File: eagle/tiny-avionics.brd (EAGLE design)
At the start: 65.8 x 25.4 mm, 67 parts, among them J1 USB-MICROB, J3 JST-PH-2-SMT-RA, U1 LP5907, U2 M25P10-AVMN6TP_TR, U3 LSM9DS0, U5 LTC1998, U6 ATMEGA32U4-AU, X1 8MHz

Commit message: Schematic work and created new device for 8-pin SPI memory chip.
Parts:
- removed C3: 4.7µ, rcl:C0603
- removed C4: .22µ, rcl:C0603
- removed R9: 0, rcl:R0603
- removed TP16, TP17: TPTP08R, testpad:TP08R
- removed U3: LSM9DS0, LSM9DS0:LGA-24
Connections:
- removed net GYR_EN: R9.1, U3.19
- removed net N$10: C4.2, U3.8
- removed net N$11: C4.1, U3.9
- removed net N$16: U3.14, U6.20
- removed net N$17: U3.13, U6.19
- removed net N$19: U3.11, U6.18
- removed net N$20: R9.2, U6.38
- removed net N$66: TP17.TP, U3.10
- removed net N$67: TP16.TP, U3.12
- removed net N$9: C3.2, U3.7
- net CLK: now also U$2.13; no longer U3.21
- net GND: now also U$2.2, U$2.3, U$2.6, U$2.7; no longer C3.1, U3.2, U3.3, U3.4, U3.5, U3.6
- net MISO: now also U$2.1; no longer U3.22, U3.23
- net MOSI: now also U$2.14; no longer U3.24
- net VCC: now also U$2.5, U$2.8; no longer U3.15, U3.16, U3.17, U3.18
- net XM_EN: now also U$2.12; no longer U3.20
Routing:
- net GYR_EN: track 28.1 -> 0.00 mm, vias 2 -> 0
- net N$17: track 18.6 -> 0.00 mm, vias 2 -> 0
- net N$16: track 18.4 -> 0.00 mm, vias 2 -> 0
- net N$19: track 14.6 -> 0.00 mm, vias 2 -> 0
- net VCC: track 141.1 -> 135.5 mm
- net GND: track 4.30 -> 0.00 mm
- net MISO: track 64.2 -> 60.5 mm
- net CLK: track 75.1 -> 71.8 mm
- net N$20: track 2.90 -> 0.00 mm
- net N$10: track 2.88 -> 0.00 mm
- net N$9: track 2.46 -> 0.00 mm
- net MOSI: track 73.6 -> 71.3 mm
- net N$11: track 1.77 -> 0.00 mm
- net N$67: track 1.42 -> 0.00 mm
- net N$66: track 1.34 -> 0.00 mm

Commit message: Working changes to schematic and layout.
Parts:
- removed U2: M25P10-AVMN6TP_TR, SOIC127P600X175-8N:SOIC127P600X175-8N
- added U$3: M25PX16, tinyav-lib:SO8
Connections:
- new net N$10: U$2.4, U6.18
- new net N$11: U$2.9, U6.19
- net CLK: now also U$3.6; no longer U2.6
- net GND: now also U$3.4; no longer U2.4
- net MEM_EN: now also U$3.1; no longer U2.1
- net MISO: now also U$3.2; no longer U2.2
- net MOSI: now also U$3.5; no longer U2.5
- net VCC: now also U$3.3, U$3.7, U$3.8; no longer U2.3, U2.7, U2.8
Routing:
- net VCC: track 135.5 -> 128.2 mm
- net CLK: track 71.8 -> 69.8 mm
- net MISO: track 60.5 -> 59.8 mm
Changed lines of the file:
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@@
 <attribute name="NAME" x="22.933" y="15.505" size="0.508" layer="25" rot="R270"/>
-</element>
-<element name="U2" library="SOIC127P600X175-8N" package="SOIC127P600X175-8N" value="M25P10-AVMN6TP_TR" x="16.682" y="6.988" smashed="yes" rot="R180">
-<attribute name="NAME" x="16.904" y="4.25" size="0.508" layer="25" rot="R180"/>
 </element>
 <element name="U5" library="tinyav-lib" package="TSOT23-6" value="LTC1998" x="17.468" y="16.136" smashed="yes" rot="R270">
@@
 <element name="R1" library="rcl" package="R0805" value="5.36k" x="-0.127" y="-15.367"/>
 <element name="U$2" library="tinyav-lib" package="LGA-14L" value="LSM6DS3" x="-4.318" y="-16.002"/>
+<element name="U$3" library="tinyav-lib" package="SO8" value="M25PX16" x="-11.43" y="-12.7"/>
 </elements>
 <signals>
@@
 <contactref element="J1" pad="MT1"/>
 <contactref element="J1" pad="MT2"/>
-<contactref element="U2" pad="4"/>
 <contactref element="C6" pad="2"/>
 <contactref element="C5" pad="2"/>
@@
 <contactref element="U$2" pad="2"/>
 <contactref element="U$2" pad="3"/>
+<contactref element="U$3" pad="4"/>
 <wire x1="61.849" y1="23.114" x2="64.008" y2="23.876" width="0" layer="19" extent="1-1"/>
 <wire x1="60.198" y1="23.876" x2="61.849" y2="23.114" width="0" layer="19" extent="1-1"/>
@@
 <wire x1="19.922" y1="12.592" x2="21.336" y2="12.827" width="0" layer="19" extent="1-1"/>
 <wire x1="17.78" y1="10.922" x2="19.922" y2="12.592" width="0" layer="19" extent="1-1"/>
-<wire x1="19.382" y1="8.893" x2="17.78" y2="10.922" width="0" layer="19" extent="1-1"/>
 <wire x1="22.86" y1="7.874" x2="22.098" y2="10.668" width="0" layer="19" extent="1-1"/>
 <wire x1="27.305" y1="5.207" x2="30.258" y2="4.806" width="0" layer="19" extent="1-1"/>
@@
 <wire x1="-4.318" y1="-16.882" x2="-3.188" y2="-16.252" width="0" layer="19" extent="1-1"/>
 <wire x1="-4.818" y1="-16.882" x2="-4.318" y2="-16.882" width="0" layer="19" extent="1-1"/>
+<wire x1="-9.525" y1="-15.3" x2="-4.818" y2="-16.882" width="0" layer="19" extent="1-1"/>
 </signal>
 <signal name="CLK">
-<contactref element="U2" pad="6"/>
 <contactref element="U6" pad="9"/>
 <wire x1="32.004" y1="6.477" x2="30.734" y2="7.874" width="0.3048" layer="16"/>
@@
 <wire x1="44.45" y1="4.572" x2="43.688" y2="3.81" width="0.3048" layer="16"/>
 <wire x1="54.746" y1="13.598" x2="54.102" y2="12.954" width="0.2794" layer="1"/>
-<wire x1="13.982" y1="7.623" x2="15.999" y2="7.623" width="0.3048" layer="1"/>
 <wire x1="15.999" y1="7.623" x2="16.256" y2="7.366" width="0.3048" layer="1"/>
 <via x="16.256" y="7.366" extent="1-16" drill="0.3302"/>
@@
 <wire x1="56.388" y1="15.24" x2="54.102" y2="12.954" width="0.3048" layer="16"/>
 <contactref element="U$2" pad="13"/>
-<wire x1="-4.318" y1="-15.122" x2="13.982" y2="7.623" width="0" layer="19" extent="1-1"/>
+<contactref element="U$3" pad="6"/>
+<wire x1="-4.318" y1="-15.122" x2="16.256" y2="7.366" width="0" layer="19" extent="1-1"/>
+<wire x1="-10.795" y1="-10.1" x2="-4.318" y2="-15.122" width="0" layer="19" extent="1-1"/>
 </signal>
 <signal name="MISO">
-<contactref element="U2" pad="2"/>
 <contactref element="U6" pad="11"/>
-<wire x1="19.382" y1="6.353" x2="20.069" y2="6.353" width="0.4064" layer="1"/>
 <wire x1="20.069" y1="6.353" x2="20.574" y2="6.858" width="0.4064" layer="1"/>
 <wire x1="20.574" y1="6.858" x2="27.178" y2="6.858" width="0.4064" layer="1"/>
@@
 <wire x1="62.357" y1="14.732" x2="63.627" y2="13.462" width="0.3048" layer="1"/>
 <contactref element="U$2" pad="1"/>
-<wire x1="-3.188" y1="-15.252" x2="19.382" y2="6.353" width="0" layer="19" extent="1-1"/>
+<contactref element="U$3" pad="2"/>
+<wire x1="-3.188" y1="-15.252" x2="-12.065" y2="-15.3" width="0" layer="19" extent="1-1"/>
+<wire x1="20.069" y1="6.353" x2="-3.188" y2="-15.252" width="0" layer="19" extent="1-1"/>
 </signal>
 <signal name="MOSI">
-<contactref element="U2" pad="5"/>
 <contactref element="U6" pad="10"/>
 <wire x1="44.856" y1="7.154" x2="44.856" y2="2.134" width="0.4064" layer="1"/>
@@
 <via x="16.51" y="8.89" extent="1-16" drill="0.3302"/>
 <wire x1="16.51" y1="8.89" x2="13.985" y2="8.89" width="0.4064" layer="1"/>
-<wire x1="13.985" y1="8.89" x2="13.982" y2="8.893" width="0.4064" layer="1"/>
 <via x="57.912" y="14.351" extent="1-16" drill="0.3302"/>
 <wire x1="52.07" y1="9.398" x2="52.07" y2="3.302" width="0.3048" layer="16"/>
@@
 <wire x1="59.563" y1="16.002" x2="61.087" y2="16.002" width="0.4064" layer="1"/>
 <contactref element="U$2" pad="14"/>
+<contactref element="U$3" pad="5"/>
 <wire x1="-3.818" y1="-15.122" x2="13.985" y2="8.89" width="0" layer="19" extent="1-1"/>
+<wire x1="-9.525" y1="-10.1" x2="-3.818" y2="-15.122" width="0" layer="19" extent="1-1"/>
 </signal>
 <signal name="MEM_EN">
-<contactref element="U2" pad="1"/>
 <contactref element="R11" pad="1"/>
 <via x="29.972" y="10.795" extent="1-16" drill="0.3302"/>
@@
 <wire x1="20.828" y1="6.096" x2="19.812" y2="5.08" width="0.4064" layer="1"/>
 <wire x1="19.812" y1="5.08" x2="19.385" y2="5.08" width="0.4064" layer="1"/>
-<wire x1="19.385" y1="5.08" x2="19.382" y2="5.083" width="0.4064" layer="1"/>
 <wire x1="31.662" y1="11.811" x2="30.988" y2="11.811" width="0.4064" layer="1"/>
 <wire x1="30.988" y1="11.811" x2="29.972" y2="10.795" width="0.4064" layer="1"/>
+<contactref element="U$3" pad="1"/>
+<wire x1="19.385" y1="5.08" x2="-13.335" y2="-15.3" width="0" layer="19" extent="1-1"/>
 </signal>
 <signal name="XM_EN">
@@
 <contactref element="C6" pad="1"/>
 <contactref element="C5" pad="1"/>
-<contactref element="U2" pad="3"/>
-<contactref element="U2" pad="7"/>
-<contactref element="U2" pad="8"/>
 <contactref element="C15" pad="1"/>
 <contactref element="C16" pad="1"/>
@@
 <wire x1="35.859" y1="16.951" x2="35.856" y2="16.954" width="0.4064" layer="1"/>
 <wire x1="35.788" y1="8.886" x2="35.856" y2="8.954" width="0.4064" layer="1"/>
-<wire x1="13.982" y1="5.083" x2="13.982" y2="6.353" width="0.6096" layer="1"/>
-<wire x1="19.382" y1="7.623" x2="18.539" y2="7.623" width="0.4064" layer="1"/>
 <wire x1="18.539" y1="7.623" x2="17.78" y2="8.382" width="0.6096" layer="1"/>
 <wire x1="17.78" y1="8.382" x2="17.78" y2="9.144" width="0.6096" layer="1"/>
@@
 <wire x1="25.908" y1="14.732" x2="25.908" y2="13.812" width="0.6096" layer="1"/>
 <wire x1="25.908" y1="13.812" x2="25.98" y2="13.74" width="0.4064" layer="1"/>
-<wire x1="13.208" y1="6.35" x2="13.979" y2="6.35" width="0.6096" layer="1"/>
-<wire x1="13.979" y1="6.35" x2="13.982" y2="6.353" width="0.6096" layer="1"/>
 <wire x1="38.862" y1="15.882" x2="38.996" y2="15.882" width="0.4064" layer="1"/>
 <wire x1="38.996" y1="15.882" x2="40.386" y2="17.272" width="0.4064" layer="1"/>
@@
 <wire x1="47.244" y1="18.542" x2="48.022" y2="18.542" width="0.4064" layer="1"/>
 <wire x1="48.022" y1="18.542" x2="48.094" y2="18.714" width="0.4064" layer="1"/>
-<wire x1="13.982" y1="6.353" x2="17.269" y2="6.353" width="0.6096" layer="1"/>
 <wire x1="17.269" y1="6.353" x2="18.539" y2="7.623" width="0.6096" layer="1"/>
 <wire x1="47.453" y1="10.551" x2="47.456" y2="10.554" width="0.4064" layer="1"/>
@@
 <wire x1="12.512" y1="4.892" x2="12.7" y2="5.08" width="0.6096" layer="1"/>
 <wire x1="12.7" y1="5.08" x2="13.979" y2="5.08" width="0.6096" layer="1"/>
-<wire x1="13.979" y1="5.08" x2="13.982" y2="5.083" width="0.6096" layer="1"/>
 <wire x1="35.856" y1="16.954" x2="33.758" y2="16.954" width="0.4064" layer="1"/>
 <wire x1="33.758" y1="16.954" x2="33.274" y2="17.438" width="0.4064" layer="1"/>
@@
 <wire x1="57.785" y1="6.604" x2="57.785" y2="10.541" width="0.6096" layer="1"/>
 <wire x1="57.785" y1="10.541" x2="56.769" y2="11.684" width="0.6096" layer="1"/>
-<contactref element="LED1" pad="4"/>
 <via x="43.434" y="23.114" extent="1-16" drill="0.3302"/>
 <via x="45.593" y="20.447" extent="1-16" drill="0.3302"/>
@@
 <wire x1="44.577" y1="22.987" x2="45.593" y2="21.971" width="0.4064" layer="16"/>
 <wire x1="45.593" y1="21.971" x2="45.593" y2="20.447" width="0.4064" layer="16"/>
-<wire x1="41.746" y1="22.562" x2="42.882" y2="22.562" width="0.4064" layer="1"/>
 <wire x1="42.882" y1="22.562" x2="43.434" y2="23.114" width="0.4064" layer="1"/>
 <wire x1="44.577" y1="22.987" x2="43.561" y2="22.987" width="0.4064" layer="16"/>
@@
 <contactref element="U$2" pad="8"/>
 <contactref element="U$2" pad="5"/>
-<wire x1="-3.818" y1="-16.882" x2="-5.438" y2="-16.752" width="0" layer="19" extent="1-1"/>
-<wire x1="9.332" y1="4.992" x2="-3.818" y2="-16.882" width="0" layer="19" extent="1-1"/>
+<contactref element="U$3" pad="8"/>
+<contactref element="U$3" pad="3"/>
+<contactref element="U$3" pad="7"/>
+<contactref element="LED1" pad="4"/>
+<wire x1="42.882" y1="22.562" x2="41.746" y2="22.562" width="0" layer="19" extent="1-1"/>
+<wire x1="13.979" y1="5.08" x2="17.269" y2="6.353" width="0" layer="19" extent="1-1"/>
+<wire x1="-3.818" y1="-16.882" x2="9.332" y2="4.992" width="0" layer="19" extent="1-1"/>
+<wire x1="-5.438" y1="-16.752" x2="-3.818" y2="-16.882" width="0" layer="19" extent="1-1"/>
+<wire x1="-10.795" y1="-15.3" x2="-5.438" y2="-16.752" width="0" layer="19" extent="1-1"/>
+<wire x1="-12.065" y1="-10.1" x2="-10.795" y2="-15.3" width="0" layer="19" extent="1-1"/>
+<wire x1="-13.335" y1="-10.1" x2="-12.065" y2="-10.1" width="0" layer="19" extent="1-1"/>
 </signal>
 <signal name="D-">
@@
 <wire x1="1.204" y1="-7.082" x2="0.823" y2="-15.367" width="0" layer="19" extent="1-1"/>
 </signal>
+<signal name="N$10">
+<contactref element="U6" pad="18"/>
+<contactref element="U$2" pad="4"/>
+<wire x1="-3.188" y1="-16.752" x2="47.456" y2="13.754" width="0" layer="19" extent="1-1"/>
+</signal>
+<signal name="N$11">
+<contactref element="U6" pad="19"/>
+<contactref element="U$2" pad="9"/>
+<wire x1="-5.438" y1="-16.252" x2="47.456" y2="14.554" width="0" layer="19" extent="1-1"/>
+</signal>
 </signals>

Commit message: Continued layout work.
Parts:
- R1, R15: device rcl:R0805 -> rcl:R0603
- moved JP2 40.9 mm to (22.9, 5.46), turned to 180 degrees
- moved U$2 37.6 mm to (20.7, 12.1), turned to 180 degrees
- moved R1 31.0 mm to (3.81, 15.4), turned to 180 degrees
- moved U$3 30.9 mm to (13.6, 5.46), turned to 90 degrees
- moved S2 30.2 mm to (56.3, 7.95)
- moved U$1 21.5 mm to (3.81, 12.8), turned to 90 degrees
- moved R17 21.5 mm to (57.0, 21.3)
- moved C17 20.5 mm to (53.5, 21.6)
- moved R2 17.8 mm to (51.7, 8.02)
- moved TP12 14.5 mm to (22.4, 19.2)
- moved C14 13.7 mm to (13.7, 14.5)
- moved TP11 12.6 mm to (24.5, 24.1)
- moved C9 12.4 mm to (27.4, 23.9)
- moved R11 11.0 mm to (35.7, 22.4)
- moved TP7 11.0 mm to (57.7, 13.3)
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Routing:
- net VCC: track 128.2 -> 29.9 mm, vias 2 -> 0
- net N$3: track 95.2 -> 0.00 mm, vias 3 -> 0
- net CLK: track 69.8 -> 16.1 mm, vias 3 -> 1
- net VBUS1: track 62.1 -> 9.09 mm, vias 4 -> 0
- net MOSI: track 71.3 -> 21.7 mm, vias 3 -> 0
- net MISO: track 59.8 -> 15.6 mm, vias 3 -> 1
- net D+: track 36.8 -> 0.00 mm
- net D-: track 33.0 -> 0.00 mm
- net FIRE_EN: track 32.1 -> 0.00 mm, vias 3 -> 0
- net XM_EN: track 28.9 -> 0.00 mm, vias 2 -> 0
- net N$5: track 19.2 -> 0.00 mm, vias 2 -> 0
- net MEM_EN: track 16.1 -> 0.00 mm, vias 2 -> 0
- net N$1: track 13.6 -> 0.00 mm, vias 2 -> 0
- net N$2: track 12.9 -> 0.00 mm
- net RED_LED: track 8.32 -> 0.00 mm
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- removed copper zone on layer 1, net VBUS1
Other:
- board text removed: "STAT2"
- board text removed: "VBAT"

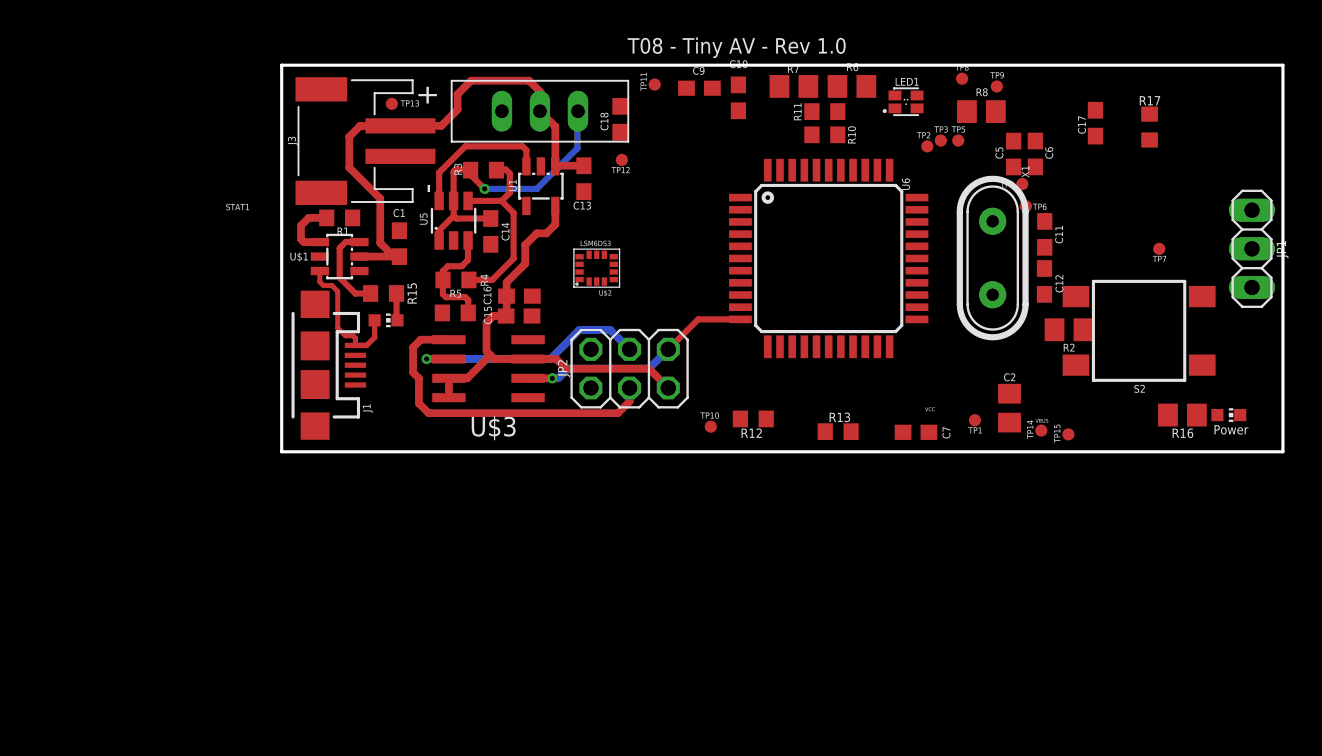
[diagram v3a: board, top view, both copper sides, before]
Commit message: More layout work.  Removed a bypass capacitor we didn't really need.
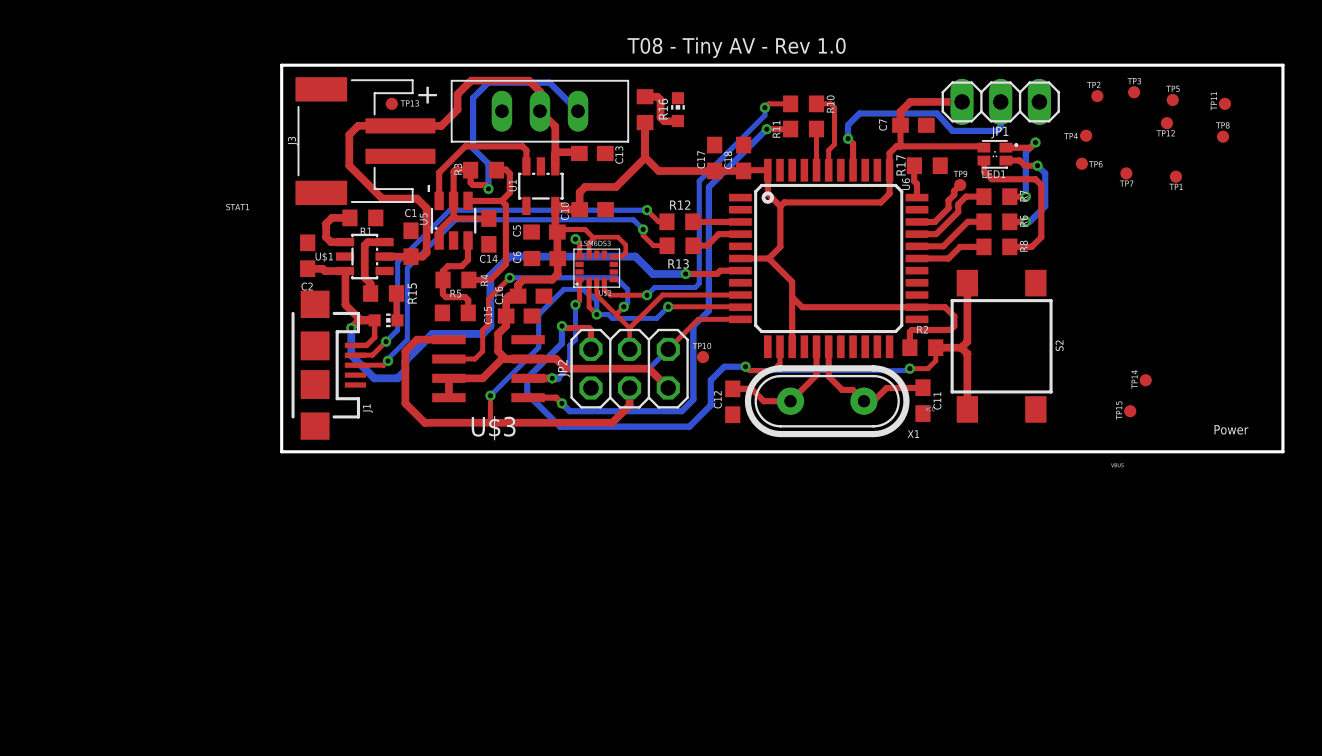
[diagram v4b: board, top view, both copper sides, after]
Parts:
- removed C9: 2.2µ, rcl:C0603
- C2: device rcl:C0805 -> rcl:C0603
- R16, R2, R6, R7, R8: device rcl:R0805 -> rcl:R0603
- moved C2 47.2 mm to (1.71, 12.9), turned to 90 degrees
- moved LED4 41.4 mm to (26.0, 22.5), turned to 0 degrees
- moved R16 40.6 mm to (23.9, 22.5), turned to 270 degrees
- moved TP11 37.5 mm to (62.0, 22.9)
- moved TP12 35.9 mm to (58.2, 21.6)
- moved C6 33.0 mm to (17.3, 12.7), turned to 180 degrees
- moved C5 31.3 mm to (17.3, 14.4), turned to 180 degrees
- moved C17 25.1 mm to (28.4, 19.3)
- moved C12 22.0 mm to (29.6, 3.29), turned to 270 degrees
- moved TP1 20.7 mm to (58.8, 18.1)
- moved C7 20.2 mm to (41.5, 21.5), turned to 0 degrees
- moved JP1 19.1 mm to (47.2, 23.0), turned to 0 degrees
- moved TP8 17.6 mm to (61.8, 20.7)
- moved R13 16.0 mm to (26.2, 13.5), turned to 180 degrees
- moved R7 15.2 mm to (47.0, 16.8), turned to 0 degrees
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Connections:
- net N$52 renamed TP3
- net N$54 renamed TP12
- net N$55 renamed TP11
- net N$56 renamed TP10
- net N$57 renamed TP9
- net N$58 renamed TP8
- net N$59 renamed TP7
- net N$60 renamed TP1
- net N$61 renamed TP2
- net N$62 renamed TP4
- net N$63 renamed TP5
- net N$64 renamed TP6
- net GND: no longer C9.2
- net VCC: no longer C9.1
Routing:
- net VCC: track 29.9 -> 114.5 mm
- net N$3: track 0.00 -> 54.2 mm, vias 0 -> 3
- net VBUS1: track 9.09 -> 45.6 mm, vias 0 -> 2
- net MEM_EN: track 0.00 -> 32.9 mm, vias 0 -> 2
- net D+: track 0.00 -> 28.2 mm, vias 0 -> 2
- net MOSI: track 21.7 -> 49.9 mm, vias 0 -> 3
- net D-: track 0.00 -> 27.3 mm, vias 0 -> 2
- net XM_EN: track 0.00 -> 22.4 mm, vias 0 -> 2
- net FIRE_EN: track 0.00 -> 15.7 mm, vias 0 -> 1
- net CLK: track 16.1 -> 31.6 mm, vias 1 -> 2
- net N$8: track 0.00 -> 10.6 mm
- net N$2: track 0.00 -> 9.18 mm
- net N$5: track 0.00 -> 8.42 mm
- net N$7: track 0.00 -> 7.84 mm, vias 0 -> 2
- net N$1: track 0.00 -> 6.96 mm, vias 0 -> 2
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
